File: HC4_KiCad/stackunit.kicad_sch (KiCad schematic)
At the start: 2 parts, among them IC10 74HC161, IC11 74HC377

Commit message: 進捗コミット2
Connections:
- net ~{CLK} renamed CLK
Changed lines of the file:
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@@
 		)
 	)
-	(global_label "~{CLK}"
+	(global_label "CLK"
 		(shape input)
 		(at 153.67 111.76 180)
@@
 		)
 	)
-	(global_label "~{CLK}"
+	(global_label "CLK"
 		(shape input)
 		(at 77.47 99.06 180)
@@
 		(on_board yes)
 		(dnp no)
-		(property "Reference" "#PWR021"
+		(property "Reference" "#PWR029"
 			(at 167.64 81.28 0)
 			(effects
@@
 			(project ""
 				(path "/33731ded-38c0-4297-bdd8-92b082f46ff8/27e10803-908c-4418-a733-f902d25b5ad6"
-					(reference "#PWR021")
+					(reference "#PWR029")
 					(unit 1)
 				)
@@
 		(dnp no)
 		(fields_autoplaced yes)
-		(property "Reference" "#PWR022"
+		(property "Reference" "#PWR030"
 			(at 167.64 129.54 0)
 			(effects
@@
 			(project ""
 				(path "/33731ded-38c0-4297-bdd8-92b082f46ff8/27e10803-908c-4418-a733-f902d25b5ad6"
-					(reference "#PWR022")
+					(reference "#PWR030")
 					(unit 1)
 				)
@@
 		(on_board yes)
 		(dnp no)
-		(property "Reference" "#PWR019"
+		(property "Reference" "#PWR027"
 			(at 92.71 85.09 0)
 			(effects
@@
 			(project "HC4_KiCad"
 				(path "/33731ded-38c0-4297-bdd8-92b082f46ff8/27e10803-908c-4418-a733-f902d25b5ad6"
-					(reference "#PWR019")
+					(reference "#PWR027")
 					(unit 1)
 				)
@@
 		(dnp no)
 		(fields_autoplaced yes)
-		(property "Reference" "#PWR020"
+		(property "Reference" "#PWR028"
 			(at 92.71 123.19 0)
 			(effects
@@
 			(project "HC4_KiCad"
 				(path "/33731ded-38c0-4297-bdd8-92b082f46ff8/27e10803-908c-4418-a733-f902d25b5ad6"
-					(reference "#PWR020")
+					(reference "#PWR028")
 					(unit 1)
 				)

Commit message: I'm tired. あとは任せた　頑張りたまえ
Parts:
- added CP8, CP9: 0.1u, Capacitor_THT:C_Disc_D3.0mm_W1.6mm_P2.50mm, symbol Device2:C_Bypass
- renumbered IC10 to IC11, IC11 to IC12
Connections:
- net GND: now also CP8.2, CP9.2
- net VCC: now also CP8.1, CP9.1
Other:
- title: (none) -> CPU

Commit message: フットプリントの割り当て修正
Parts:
- IC11: footprint (none) -> Package_DIP:DIP-16_W7.62mm_Socket
- IC12: footprint (none) -> Package_DIP:DIP-20_W7.62mm_Socket
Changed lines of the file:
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@@
 	(label "Level_B3"
 		(at 189.23 96.52 180)
+		(fields_autoplaced yes)
 		(effects
 			(font
@@
 	(label "Stack_IN0"
 		(at 69.85 102.87 0)
+		(fields_autoplaced yes)
 		(effects
 			(font
@@
 	(label "Level_B2"
 		(at 146.05 101.6 0)
+		(fields_autoplaced yes)
 		(effects
 			(font
@@
 	(label "Level_A0"
 		(at 146.05 88.9 0)
+		(fields_autoplaced yes)
 		(effects
 			(font
@@
 	(label "Level_A2"
 		(at 111.76 107.95 180)
+		(fields_autoplaced yes)
 		(effects
 			(font
@@
 	(label "Level_A1"
 		(at 146.05 91.44 0)
+		(fields_autoplaced yes)
 		(effects
 			(font
@@
 	(label "Level_B2"
 		(at 189.23 93.98 180)
+		(fields_autoplaced yes)
 		(effects
 			(font
@@
 	(label "Stack_IN3"
 		(at 69.85 110.49 0)
+		(fields_autoplaced yes)
 		(effects
 			(font
@@
 	(label "Level_C3"
 		(at 189.23 106.68 180)
+		(fields_autoplaced yes)
 		(effects
 			(font
@@
 	(label "Level_A3"
 		(at 146.05 96.52 0)
+		(fields_autoplaced yes)
 		(effects
 			(font
@@
 	(label "Level_A1"
 		(at 111.76 105.41 180)
+		(fields_autoplaced yes)
 		(effects
 			(font
@@
 	(label "Level_C0"
 		(at 189.23 99.06 180)
+		(fields_autoplaced yes)
 		(effects
 			(font
@@
 	(label "Level_B3"
 		(at 146.05 99.06 0)
+		(fields_autoplaced yes)
 		(effects
 			(font
@@
 	(label "Level_B1"
 		(at 189.23 91.44 180)
+		(fields_autoplaced yes)
 		(effects
 			(font
@@
 	(label "Level_B1"
 		(at 146.05 104.14 0)
+		(fields_autoplaced yes)
 		(effects
 			(font
@@
 	(label "Level_A3"
 		(at 111.76 110.49 180)
+		(fields_autoplaced yes)
 		(effects
 			(font
@@
 	(label "Level_B0"
 		(at 189.23 88.9 180)
+		(fields_autoplaced yes)
 		(effects
 			(font
@@
 	(label "Level_C2"
 		(at 189.23 104.14 180)
+		(fields_autoplaced yes)
 		(effects
 			(font
@@
 	(label "Level_A0"
 		(at 111.76 102.87 180)
+		(fields_autoplaced yes)
 		(effects
 			(font
@@
 	(label "Level_B0"
 		(at 146.05 106.68 0)
+		(fields_autoplaced yes)
 		(effects
 			(font
@@
 	(label "Stack_IN2"
 		(at 69.85 107.95 0)
+		(fields_autoplaced yes)
 		(effects
 			(font
@@
 	(label "Stack_IN1"
 		(at 69.85 105.41 0)
+		(fields_autoplaced yes)
 		(effects
 			(font
@@
 	(label "Level_C1"
 		(at 189.23 101.6 180)
+		(fields_autoplaced yes)
 		(effects
 			(font
@@
 	(label "Level_A2"
 		(at 146.05 93.98 0)
+		(fields_autoplaced yes)
 		(effects
 			(font
@@
 		(shape output)
 		(at 118.11 78.74 0)
+		(fields_autoplaced yes)
 		(effects
 			(font
@@
 		(shape output)
 		(at 194.31 101.6 0)
+		(fields_autoplaced yes)
 		(effects
 			(font
@@
 		(shape output)
 		(at 194.31 78.74 0)
+		(fields_autoplaced yes)
 		(effects
 			(font
@@
 		(shape input)
 		(at 152.4 114.3 180)
+		(fields_autoplaced yes)
 		(effects
 			(font
@@
 		(shape input)
 		(at 80.01 91.44 180)
+		(fields_autoplaced yes)
 		(effects
 			(font
@@
 		(shape input)
 		(at 66.04 99.06 180)
+		(fields_autoplaced yes)
 		(effects
 			(font
@@
 			)
 		)
-		(property "Footprint" ""
+		(property "Footprint" "Package_DIP:DIP-20_W7.62mm_Socket"
 			(at 167.64 101.6 0)
 			(effects
@@
 			)
 		)
-		(property "Footprint" ""
+		(property "Footprint" "Package_DIP:DIP-16_W7.62mm_Socket"
 			(at 92.71 83.82 0)
 			(effects

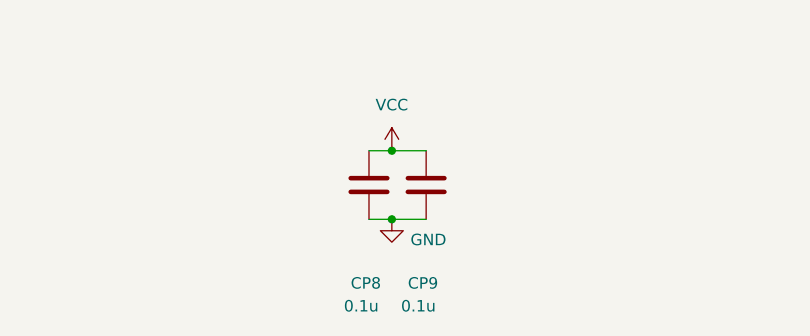
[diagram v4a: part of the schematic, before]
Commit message: ICの配置を再検討
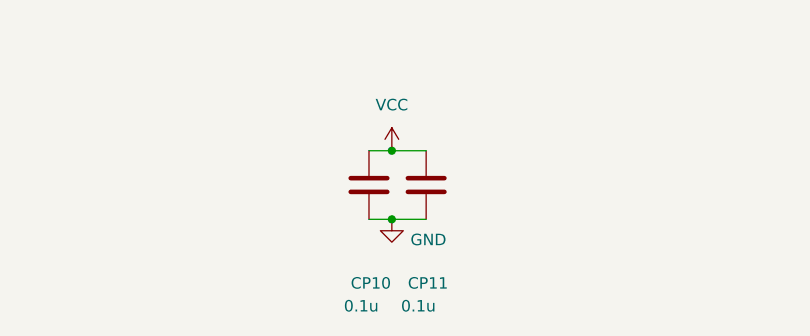
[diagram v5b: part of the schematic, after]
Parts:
- renumbered CP8 to CP10, CP9 to CP11
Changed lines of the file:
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@@
 	(label "Level_B3"
 		(at 189.23 96.52 180)
-		(fields_autoplaced yes)
 		(effects
 			(font
@@
 	(label "Stack_IN0"
 		(at 69.85 102.87 0)
-		(fields_autoplaced yes)
 		(effects
 			(font
@@
 	(label "Level_B2"
 		(at 146.05 101.6 0)
-		(fields_autoplaced yes)
 		(effects
 			(font
@@
 	(label "Level_A0"
 		(at 146.05 88.9 0)
-		(fields_autoplaced yes)
 		(effects
 			(font
@@
 	(label "Level_A2"
 		(at 111.76 107.95 180)
-		(fields_autoplaced yes)
 		(effects
 			(font
@@
 	(label "Level_A1"
 		(at 146.05 91.44 0)
-		(fields_autoplaced yes)
 		(effects
 			(font
@@
 	(label "Level_B2"
 		(at 189.23 93.98 180)
-		(fields_autoplaced yes)
 		(effects
 			(font
@@
 	(label "Stack_IN3"
 		(at 69.85 110.49 0)
-		(fields_autoplaced yes)
 		(effects
 			(font
@@
 	(label "Level_C3"
 		(at 189.23 106.68 180)
-		(fields_autoplaced yes)
 		(effects
 			(font
@@
 	(label "Level_A3"
 		(at 146.05 96.52 0)
-		(fields_autoplaced yes)
 		(effects
 			(font
@@
 	(label "Level_A1"
 		(at 111.76 105.41 180)
-		(fields_autoplaced yes)
 		(effects
 			(font
@@
 	(label "Level_C0"
 		(at 189.23 99.06 180)
-		(fields_autoplaced yes)
 		(effects
 			(font
@@
 	(label "Level_B3"
 		(at 146.05 99.06 0)
-		(fields_autoplaced yes)
 		(effects
 			(font
@@
 	(label "Level_B1"
 		(at 189.23 91.44 180)
-		(fields_autoplaced yes)
 		(effects
 			(font
@@
 	(label "Level_B1"
 		(at 146.05 104.14 0)
-		(fields_autoplaced yes)
 		(effects
 			(font
@@
 	(label "Level_A3"
 		(at 111.76 110.49 180)
-		(fields_autoplaced yes)
 		(effects
 			(font
@@
 	(label "Level_B0"
 		(at 189.23 88.9 180)
-		(fields_autoplaced yes)
 		(effects
 			(font
@@
 	(label "Level_C2"
 		(at 189.23 104.14 180)
-		(fields_autoplaced yes)
 		(effects
 			(font
@@
 	(label "Level_A0"
 		(at 111.76 102.87 180)
-		(fields_autoplaced yes)
 		(effects
 			(font
@@
 	(label "Level_B0"
 		(at 146.05 106.68 0)
-		(fields_autoplaced yes)
 		(effects
 			(font
@@
 	(label "Stack_IN2"
 		(at 69.85 107.95 0)
-		(fields_autoplaced yes)
 		(effects
 			(font
@@
 	(label "Stack_IN1"
 		(at 69.85 105.41 0)
-		(fields_autoplaced yes)
 		(effects
 			(font
@@
 	(label "Level_C1"
 		(at 189.23 101.6 180)
-		(fields_autoplaced yes)
 		(effects
 			(font
@@
 	(label "Level_A2"
 		(at 146.05 93.98 0)
-		(fields_autoplaced yes)
 		(effects
 			(font
@@
 		(shape output)
 		(at 118.11 78.74 0)
-		(fields_autoplaced yes)
 		(effects
 			(font
@@
 		(shape output)
 		(at 194.31 101.6 0)
-		(fields_autoplaced yes)
 		(effects
 			(font
@@
 		(shape output)
 		(at 194.31 78.74 0)
-		(fields_autoplaced yes)
 		(effects
 			(font
@@
 		(shape input)
 		(at 152.4 114.3 180)
-		(fields_autoplaced yes)
 		(effects
 			(font
@@
 		(shape input)
 		(at 80.01 91.44 180)
-		(fields_autoplaced yes)
 		(effects
 			(font
@@
 		(shape input)
 		(at 66.04 99.06 180)
-		(fields_autoplaced yes)
 		(effects
 			(font
@@
 		(on_board yes)
 		(dnp no)
-		(property "Reference" "CP8"
+		(property "Reference" "CP10"
 			(at 95.758 160.782 0)
 			(effects
@@
 			(project "HC4_KiCad"
 				(path "/33731ded-38c0-4297-bdd8-92b082f46ff8/27e10803-908c-4418-a733-f902d25b5ad6"
-					(reference "CP8")
+					(reference "CP10")
 					(unit 1)
 				)
@@
 		(on_board yes)
 		(dnp no)
-		(property "Reference" "CP9"
+		(property "Reference" "CP11"
 			(at 102.108 160.782 0)
 			(effects
@@
 			(project "HC4_KiCad"
 				(path "/33731ded-38c0-4297-bdd8-92b082f46ff8/27e10803-908c-4418-a733-f902d25b5ad6"
-					(reference "CP9")
+					(reference "CP11")
 					(unit 1)
 				)

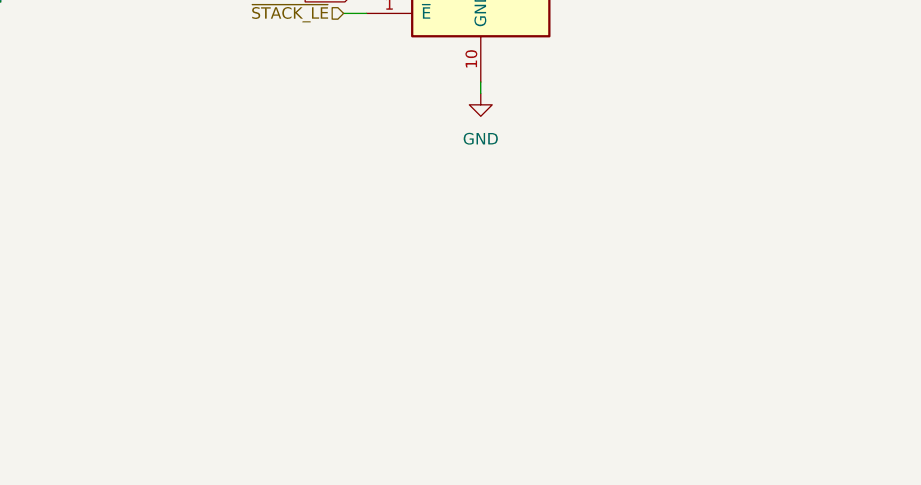
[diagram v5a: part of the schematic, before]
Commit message: StackLEDつけた
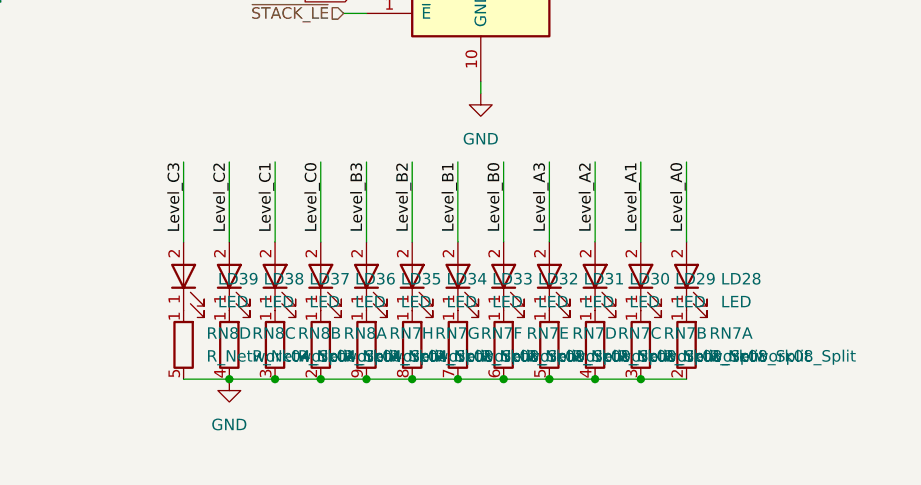
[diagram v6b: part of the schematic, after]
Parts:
- added LD28, LD29, LD30, LD31, LD32, LD33, LD34, LD35, LD36, LD37, LD38, LD39: LED, LED_THT:LED_Rectangular_W5.0mm_H2.0mm, symbol Device2:LED_
- added RN7: R_Network08_Split, Resistor_THT:R_Array_SIP9, symbol Device:R_Network08_Split
- added RN8: R_Network04_Split, Resistor_THT:R_Array_SIP5, symbol Device:R_Network04_Split
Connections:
- net GND: now also RN7.2 (R1.2), RN7.3 (R2.2), RN7.4 (R3.2), RN7.5 (R4.2), RN7.6 (R5.2), RN7.7 (R6.2), RN7.8 (R7.2), RN7.9 (R8.2), RN8.2 (R1.2), RN8.3 (R2.2), RN8.4 (R3.2), RN8.5 (R4.2)
- net Level_A0: now also LD28.2
- net Level_A1: now also LD29.2
- net Level_A2: now also LD30.2
- net Level_A3: now also LD31.2
- net Level_B0: now also LD32.2
- net Level_B1: now also LD33.2
- net Level_B2: now also LD34.2
- net Level_B3: now also LD35.2
- net Level_C0: now also LD36.2
- net Level_C1: now also LD37.2
- net Level_C2: now also LD38.2
- net Level_C3: now also LD39.2
- new net: LD37.1 (K), RN8.1 (R1)
- new net: LD36.1 (K), RN8.1 (R1)
- new net: LD28.1 (K), RN7.1 (R1)
- new net: LD29.1 (K), RN7.1 (R1)
- new net: LD35.1 (K), RN7.1 (R1)
- new net: LD30.1 (K), RN7.1 (R1)
- new net: LD32.1 (K), RN7.1 (R1)
- new net: LD39.1 (K), RN8.1 (R1)
- new net: LD31.1 (K), RN7.1 (R1)
- new net: LD33.1 (K), RN7.1 (R1)
- new net: LD34.1 (K), RN7.1 (R1)
- new net: LD38.1 (K), RN8.1 (R1)

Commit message: 電源配線ほぼ完了
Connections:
- net GND: now also RN7.1 (R1), RN7.1 (R1), RN7.1 (R1), RN7.1 (R1), RN7.1 (R1), RN7.1 (R1), RN7.1 (R1), RN7.1 (R1), RN8.1 (R1), RN8.1 (R1), RN8.1 (R1), RN8.1 (R1); no longer RN7.2 (R1.2), RN7.3 (R2.2), RN7.4 (R3.2), RN7.5 (R4.2), RN7.6 (R5.2), RN7.7 (R6.2), RN7.8 (R7.2), RN7.9 (R8.2), RN8.2 (R1.2), RN8.3 (R2.2), RN8.4 (R3.2), RN8.5 (R4.2)
- net at LD37.1 (K): now also RN8.3 (R2.2); no longer RN8.1 (R1)
- net at LD36.1 (K): now also RN8.2 (R1.2); no longer RN8.1 (R1)
- net at LD28.1 (K): now also RN7.2 (R1.2); no longer RN7.1 (R1)
- net at LD29.1 (K): now also RN7.3 (R2.2); no longer RN7.1 (R1)
- net at LD35.1 (K): now also RN7.9 (R8.2); no longer RN7.1 (R1)
- net at LD30.1 (K): now also RN7.4 (R3.2); no longer RN7.1 (R1)
- net at LD32.1 (K): now also RN7.6 (R5.2); no longer RN7.1 (R1)
- net at LD39.1 (K): now also RN8.5 (R4.2); no longer RN8.1 (R1)
- net at LD31.1 (K): now also RN7.5 (R4.2); no longer RN7.1 (R1)
- net at LD33.1 (K): now also RN7.7 (R6.2); no longer RN7.1 (R1)
- net at LD34.1 (K): now also RN7.8 (R7.2); no longer RN7.1 (R1)
- net at LD38.1 (K): now also RN8.4 (R3.2); no longer RN8.1 (R1)
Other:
- moved on the sheet: RN7A, RN7B, RN7C, RN7D, RN7E, RN7F, RN7G, RN7H, RN8A, RN8B, RN8C, RN8D

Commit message: またも手直し
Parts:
- renumbered LD37 to LD10, LD36 to LD11, LD35 to LD12, LD34 to LD13, LD33 to LD14, LD32 to LD15, LD31 to LD16, LD30 to LD17, LD29 to LD18, LD28 to LD19, LD39 to LD8, LD38 to LD9, RN8 to RN3, RN7 to RN4
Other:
- title: CPU -> HC4_CPU
